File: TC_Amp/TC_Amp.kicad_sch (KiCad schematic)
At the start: 20 parts, among them J2 Screw_Terminal_01x04, U1 LT1025CN8-PBF, U2 LTC1049CN8_PBF, U3 LT1054, U4 LM741, U5 LTC1049CN8_PBF

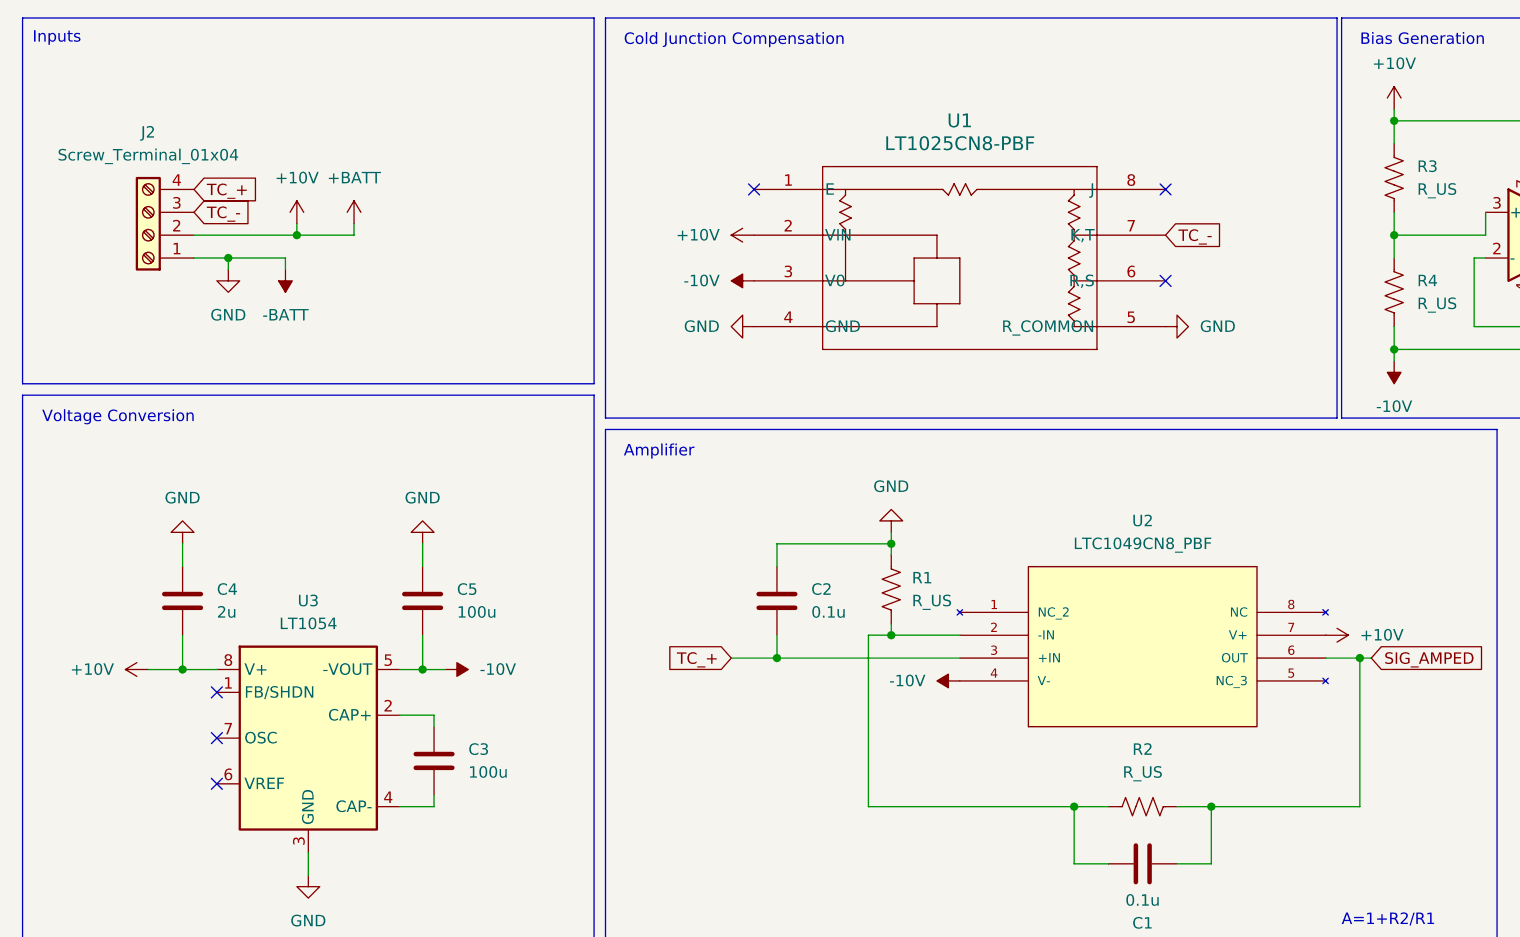
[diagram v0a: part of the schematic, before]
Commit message: seperated screw terminals
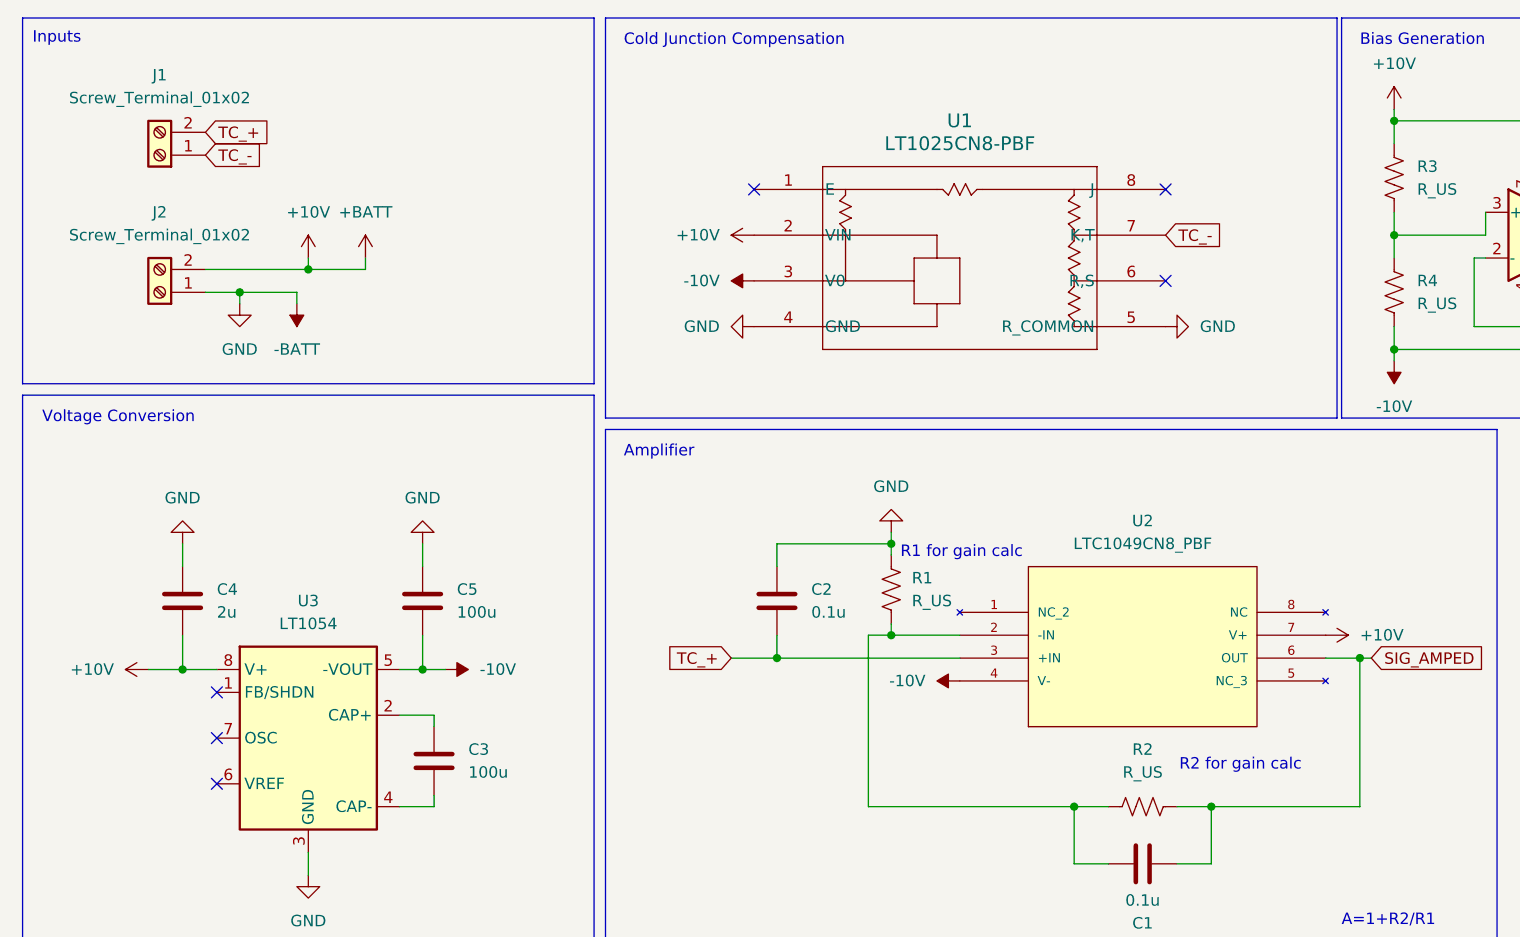
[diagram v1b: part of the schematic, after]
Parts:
- removed J2: Screw_Terminal_01x04, symbol Connector:Screw_Terminal_01x04
- added J1, J2: Screw_Terminal_01x02, symbol Connector:Screw_Terminal_01x02
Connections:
- net +10V: now also J2.2 (Pin_2)
- net -BATT: now also J2.1 (Pin_1)
- net TC_+: now also J1.2 (Pin_2)
- net TC_-: now also J1.1 (Pin_1)
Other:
- note added: "R1 for gain calc"
- note added: "R2 for gain calc"

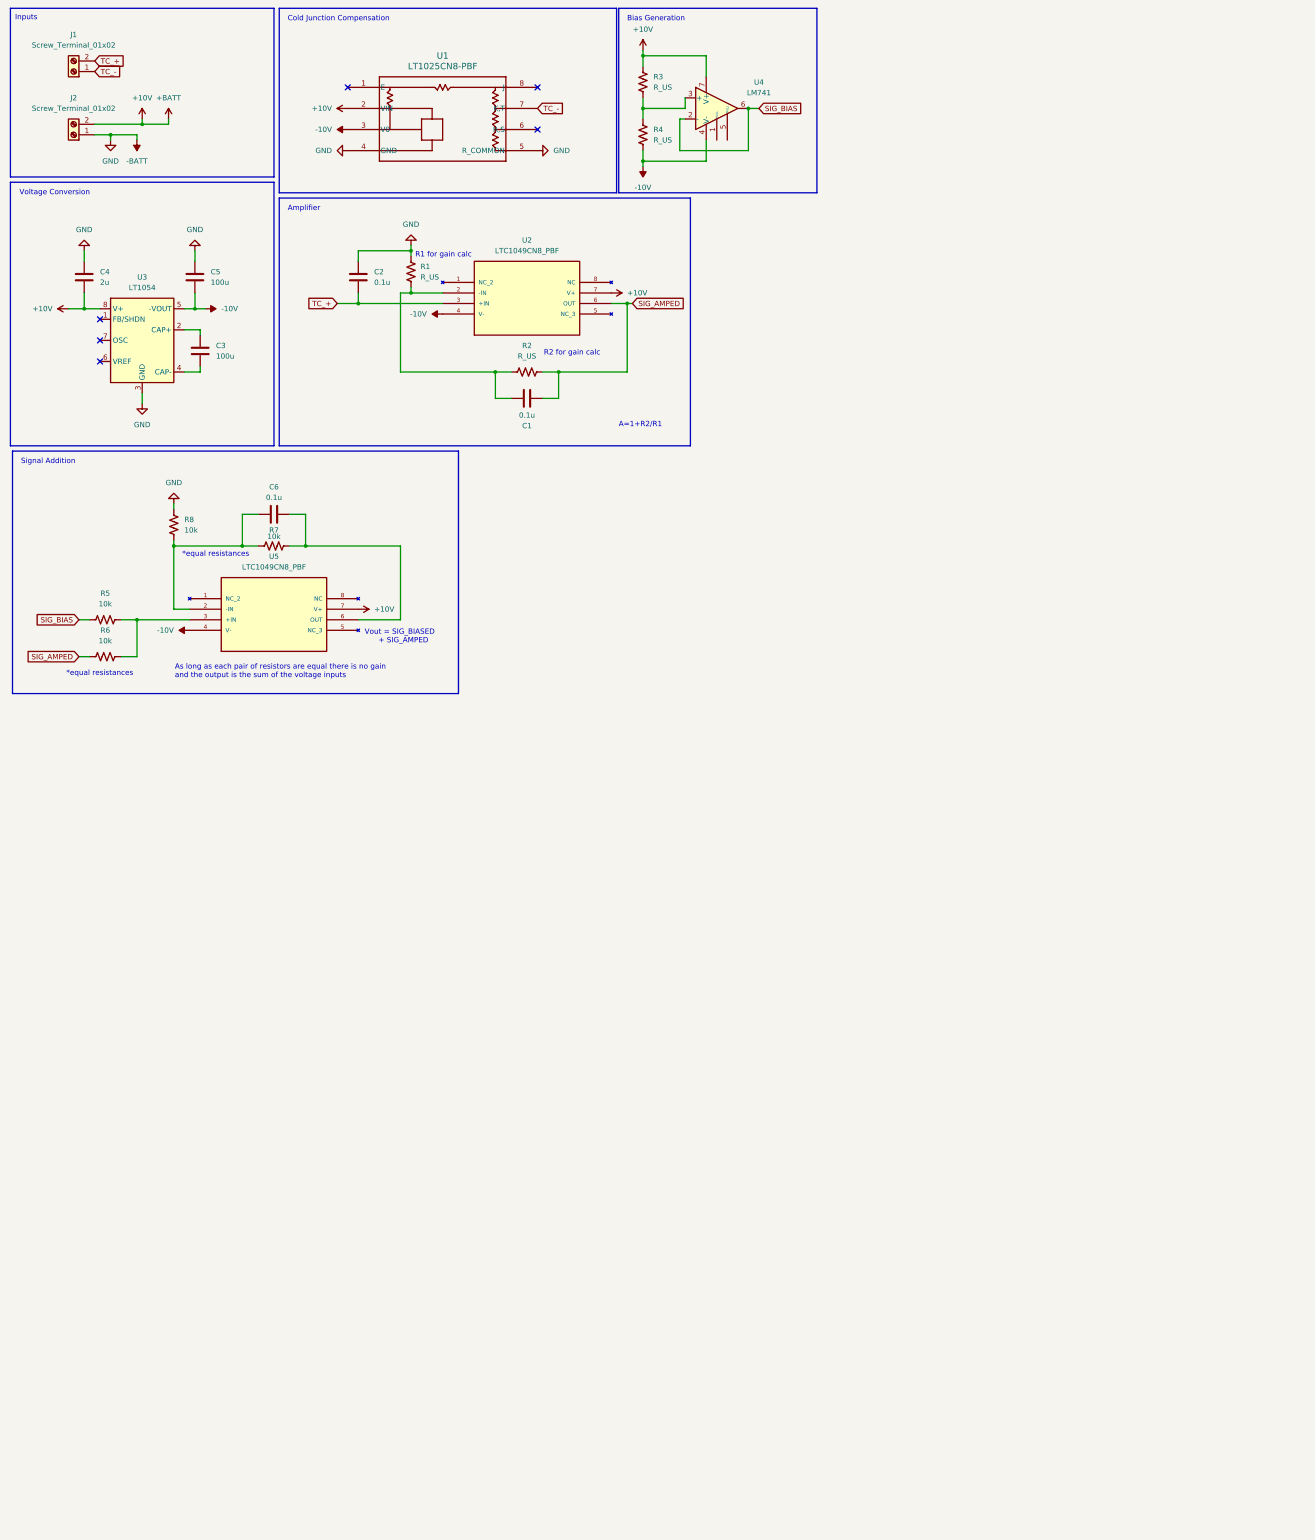
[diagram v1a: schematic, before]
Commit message: changed to 5v regulation
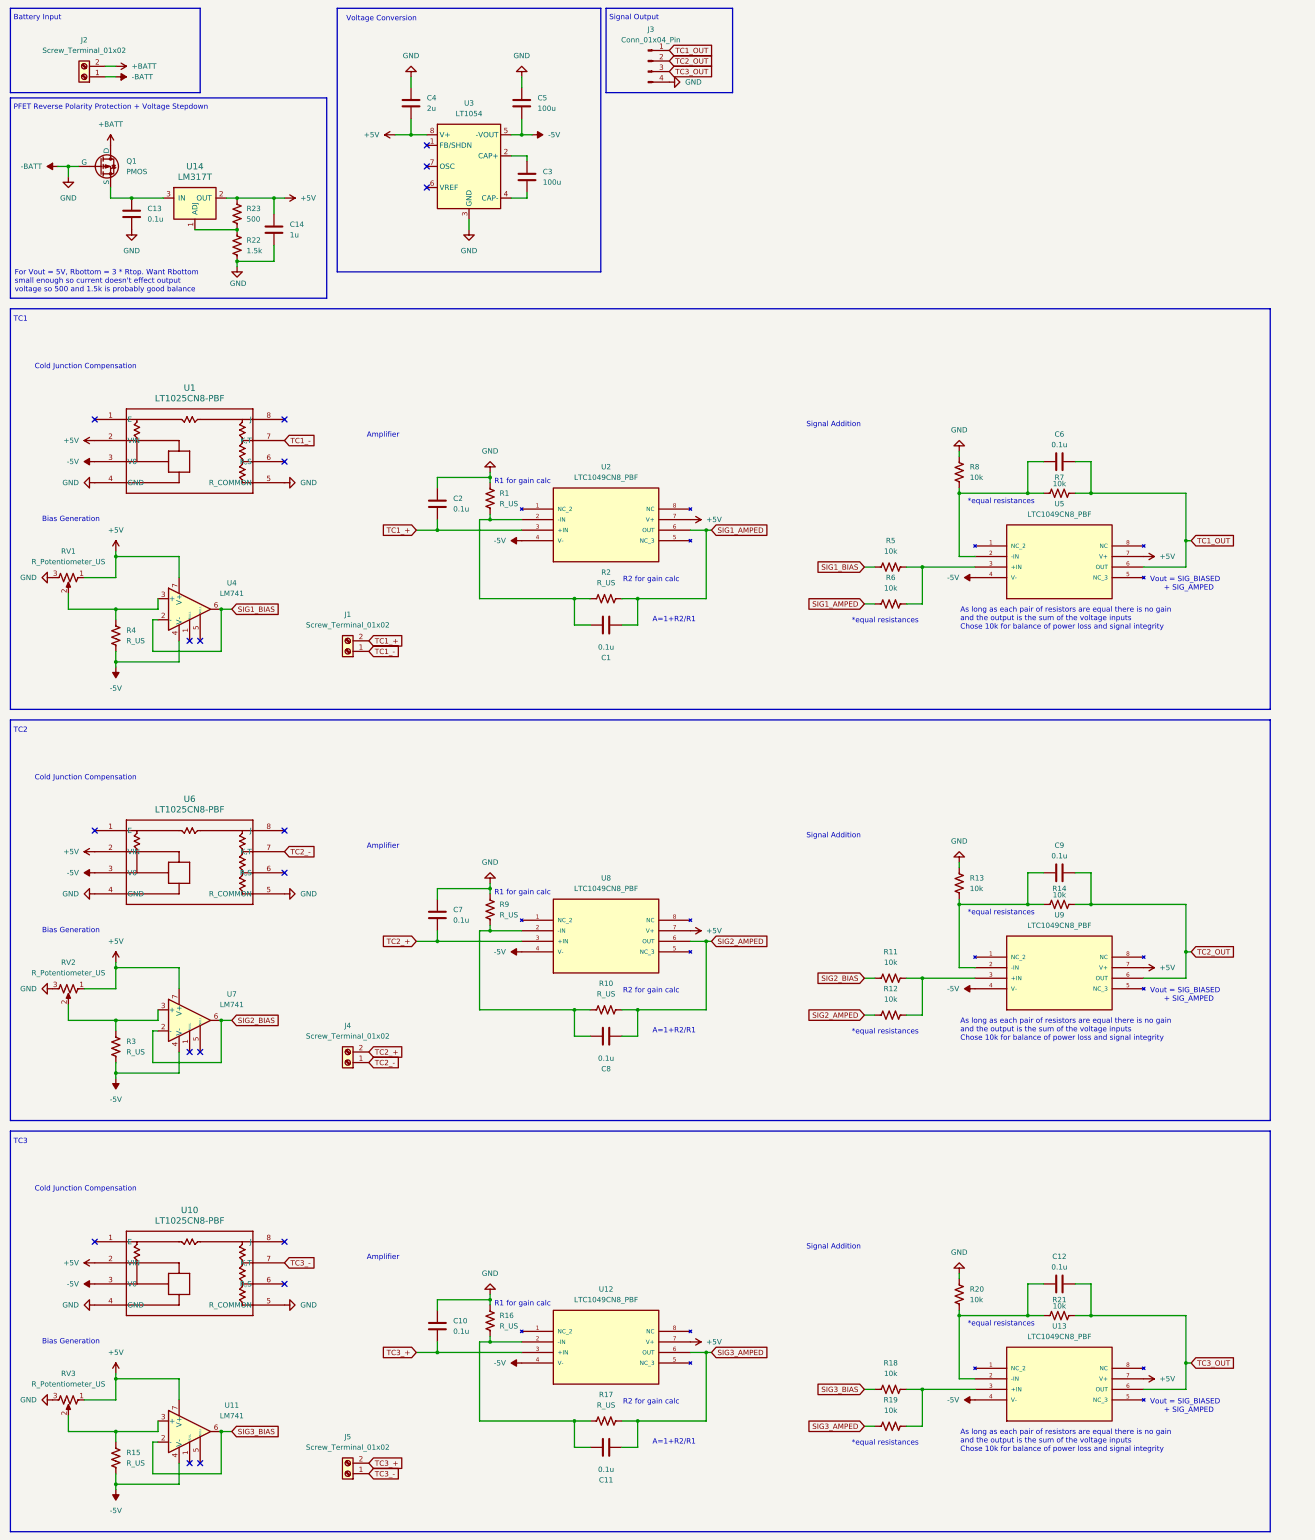
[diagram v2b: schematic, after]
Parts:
- added C10, C11, C12, C13, C7, C8, C9: 0.1u, Capacitor_THT:C_Radial_D5.0mm_H5.0mm_P2.00mm, symbol Device:C
- added C14: 1u, Capacitor_THT:C_Radial_D5.0mm_H5.0mm_P2.00mm, symbol Device:C
- added J3: Conn_01x04_Pin, Connector_PinHeader_2.54mm:PinHeader_1x04_P2.54mm_Vertical, symbol Connector:Conn_01x04_Pin
- added J4, J5: Screw_Terminal_01x02, Footprints:TC_SOCKET, symbol Connector:Screw_Terminal_01x02
- added Q1: PMOS, Footprints:PFET_VERT, symbol Simulation_SPICE:PMOS
- added R10, R15, R16, R17, R9: R_US, Resistor_THT:R_Axial_DIN0207_L6.3mm_D2.5mm_P10.16mm_Horizontal, symbol Device:R_US
- added R11, R12, R13, R14, R18, R19, R20, R21: 10k, Resistor_THT:R_Axial_DIN0207_L6.3mm_D2.5mm_P10.16mm_Horizontal, symbol Device:R_US
- added R22: 1.5k, Resistor_THT:R_Axial_DIN0207_L6.3mm_D2.5mm_P10.16mm_Horizontal, symbol Device:R_US
- added R23: 500, Resistor_THT:R_Axial_DIN0207_L6.3mm_D2.5mm_P10.16mm_Horizontal, symbol Device:R_US
- added RV1, RV2, RV3: R_Potentiometer_US, Potentiometer_THT:Potentiometer_Bourns_3386W_Horizontal, symbol Device:R_Potentiometer_US
- added U10, U6: LT1025CN8-PBF, Footprints:PDIP8_LT1025CN8-PBF_ADI, symbol 2025-02-03_00-05-09:LT1025CN8-PBF
- added U11, U7: LM741, Footprints:J08A_TEX, symbol Amplifier_Operational:LM741
- added U12, U13, U8, U9: LTC1049CN8_PBF, Footprints:PDIP-8_N, symbol LTC1049CN8_PBF:LTC1049CN8_PBF
- added U14: LM317T, digikey-footprints:TO-220-3, symbol dk_PMIC-Voltage-Regulators-Linear:LM317T
- C1, C2, C3, C4, C5, C6: footprint (none) -> Capacitor_THT:C_Radial_D5.0mm_H5.0mm_P2.00mm
- J1: footprint (none) -> Footprints:TC_SOCKET
- J2: footprint (none) -> TerminalBlock:TerminalBlock_bornier-2_P5.08mm
- R1, R2, R3, R4, R5, R6, R7, R8: footprint (none) -> Resistor_THT:R_Axial_DIN0207_L6.3mm_D2.5mm_P10.16mm_Horizontal
- U1: footprint PDIP8_LT1025CN8-PBF_ADI -> Footprints:PDIP8_LT1025CN8-PBF_ADI
- U2, U5: footprint LTC1049CN8_PBF:PDIP-8_N -> Footprints:PDIP-8_N
- U3: footprint (none) -> Footprints:DIP794W45P254L959H508Q8
- U4: footprint (none) -> Footprints:J08A_TEX
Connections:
- net -BATT: now also C10.1, C13.2, C14.2, C7.1, J3.4 (Pin_4), Q1.2 (G), R13.2, R16.1, R20.2, R22.2, R9.1, RV1.3, RV2.3, RV3.3, U10.4 (GND), U10.5 (R_COMMON), U6.4 (GND), U6.5 (R_COMMON)
- net TC1_OUT: now reaches C6.1, R7.2, U5.6 (OUT)
- net TC1_OUT: now also J3.1 (Pin_1)
- net at R4.2, U4.3 (+): now also RV1.2; no longer R3.2
- net +10V renamed +5V
- net +5V: now also C14.1, R23.1, RV1.1, RV2.1, RV3.1, U10.2 (VIN), U11.7 (V+), U12.7 (V+), U13.7 (V+), U14.2 (OUT), U6.2 (VIN), U7.7 (V+), U8.7 (V+), U9.7 (V+); no longer J2.2 (Pin_2), R3.1
- net -10V renamed -5V
- net -5V: now also R3.1, R15.1, U10.3 (V0), U11.4 (V-), U12.4 (V-), U13.4 (V-), U6.3 (V0), U7.4 (V-), U8.4 (V-), U9.4 (V-)
- net SIG_AMPED renamed SIG1_AMPED
- net SIG_BIAS renamed SIG1_BIAS
- net TC_+ renamed TC1_+
- net TC_- renamed TC1_-
- new net: R18.2, R19.2, U13.3 (+IN)
- new net: C13.1, Q1.3 (S), U14.3 (IN)
- new net: C9.2, R13.1, R14.1, U9.2 (-IN)
- new net: C11.1, R16.2, R17.1, U12.2 (-IN)
- new net: R11.2, R12.2, U9.3 (+IN)
- new net: C8.1, R10.1, R9.2, U8.2 (-IN)
- new net: R3.2, RV2.2, U7.3 (+)
- new net: R15.2, RV3.2, U11.3 (+)
- new net: R22.1, R23.2, U14.1 (ADJ)
- new net: C12.2, R20.1, R21.1, U13.2 (-IN)
- new net +BATT: J2.2 (Pin_2), Q1.1 (D)
- new net SIG2_AMPED: C8.2, R10.2, R12.1, U8.6 (OUT)
- new net SIG2_BIAS: R11.1, U7.2 (-), U7.6
- new net SIG3_AMPED: C11.2, R17.2, R19.1, U12.6 (OUT)
- new net SIG3_BIAS: R18.1, U11.2 (-), U11.6
- new net TC2_+: C7.2, J4.2 (Pin_2), U8.3 (+IN)
- new net TC2_-: J4.1 (Pin_1), U6.7 (K,T)
- new net TC2_OUT: C9.1, J3.2 (Pin_2), R14.2, U9.6 (OUT)
- new net TC3_+: C10.2, J5.2 (Pin_2), U12.3 (+IN)
- new net TC3_-: J5.1 (Pin_1), U10.7 (K,T)
- new net TC3_OUT: C12.1, J3.3 (Pin_3), R21.2, U13.6 (OUT)
- no-connect marks 6 -> 18
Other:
- note added: "As long as each pair of resistors are equal there is no gain and the output is the sum of the voltage inputs Chose 10k for balance of power loss and signal integrity"
- note added: "Battery Input"
- note added: "For Vout = 5V, Rbottom = 3 * Rtop. Want Rbottom small enough so current doesn't effect output voltage so 500 and 1.5k is probably good balance"
- note added: "PFET Reverse Polarity Protection + Voltage Stepdown"
- note added: "Signal Output"
- note added: "TC1"
- note added: "TC2"
- note added: "TC3"
- note removed: "As long as each pair of resistors are equal there is no gain and the output is the sum of the voltage inputs"
- note removed: "Inputs"
- moved on the sheet: C1, C2, C3, C4, C5, C6, J1, J2, R1, R2, R4, R5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

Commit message: change to common cjc
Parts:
- removed U1, U10, U6: LT1025CN8-PBF, Footprints:PDIP8_LT1025CN8-PBF_ADI, symbol 2025-02-03_00-05-09:LT1025CN8-PBF
- added U15: LT1025CN8-PBF, Footprints:PDIP8_LT1025CN8-PBF_ADI, symbol 2025-02-03_00-05-09:LT1025CN8-PBF
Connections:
- net TC2_- is gone; now on net TC1_-: J4.1 (Pin_1)
- net TC3_- is gone; now on net TC1_-: J5.1 (Pin_1)
- net +5V: now also U15.2 (VIN)
- net -5V: now also U15.3 (V0)
- net -BATT: now also U15.4 (GND), U15.5 (R_COMMON)
- net TC1_-: now also U15.7 (K,T)
- no-connect marks 18 -> 12
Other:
- moved on the sheet: C1, C10, C11, C12, C13, C14, C2, C3, C4, C5, C6, C7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

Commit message: finished prelim traces
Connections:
- net TC1_OUT: now also J3.3 (Pin_3); no longer J3.1 (Pin_1)
- net TC3_OUT: now also J3.1 (Pin_1); no longer J3.3 (Pin_3)
